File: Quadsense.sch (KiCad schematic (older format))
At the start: 45 parts, among them IC1 BME280, IC2 AP7330, IC3 ADC_LTC2497, P1 CONN_6, P2 CONN_6, P3 CONN_6, P4 CONN_6, P5 CONN_8, Q1 AO3418

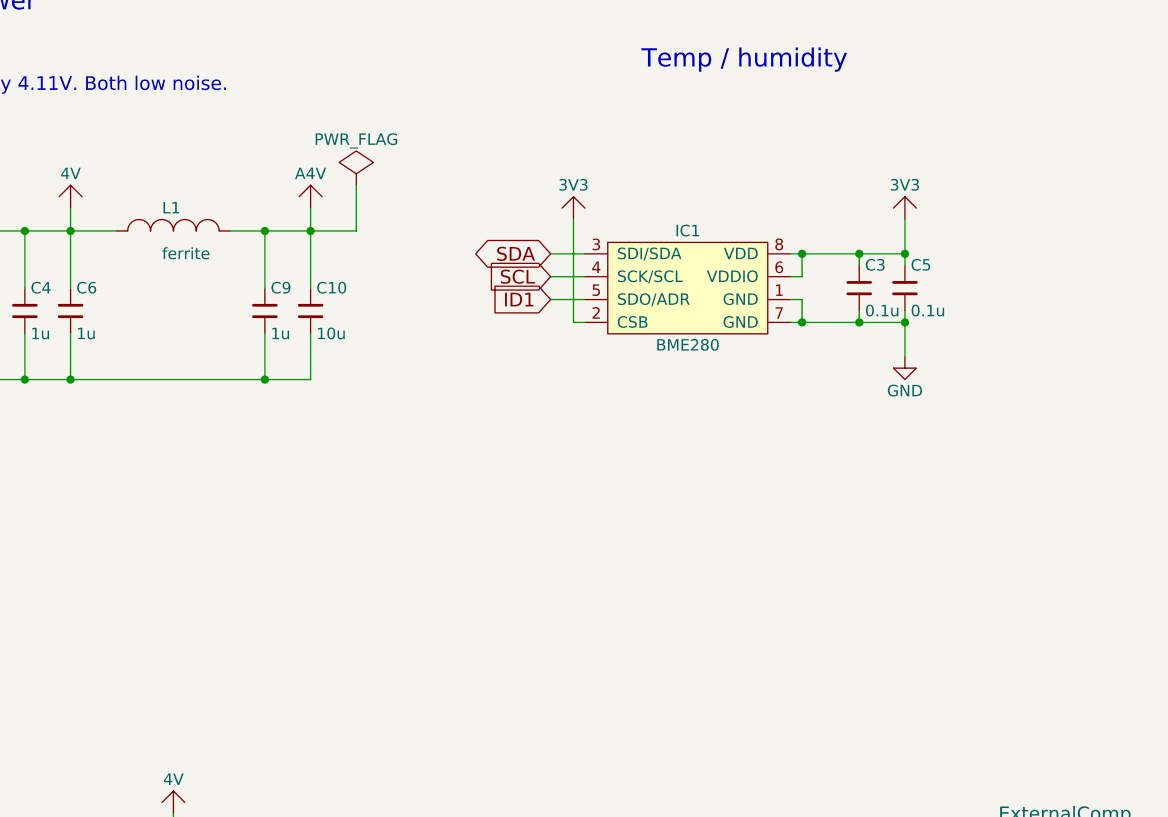
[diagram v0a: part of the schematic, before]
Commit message: Added second BME280, fixed footprints, better analog decoupling, resized module board
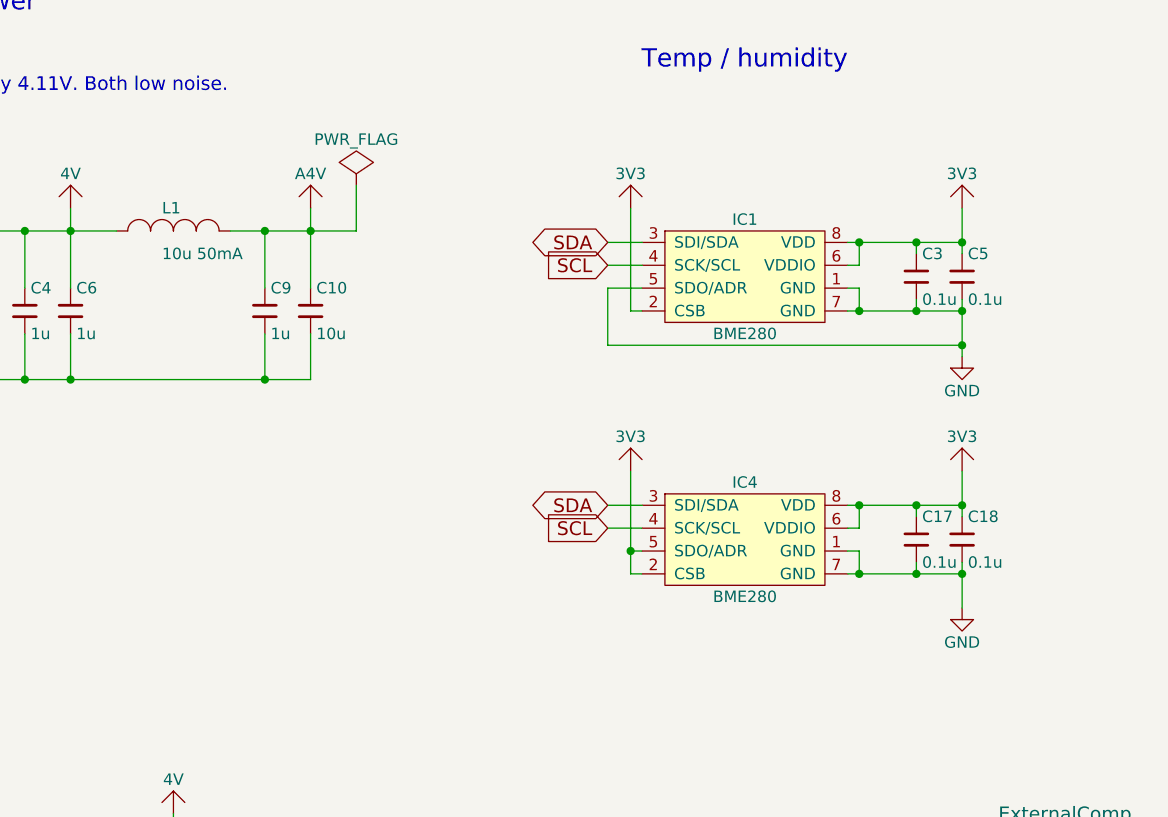
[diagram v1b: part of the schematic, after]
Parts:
- added C17, C18: 0.1u, everykey:0603, symbol C
- added IC4: BME280, everykey:BME280, symbol BME280
- L1: value ferrite -> 10u 50mA
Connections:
- net 3V3: now also C17.1, C18.1, IC4.2 (CSB), IC4.5 (SDO/ADR), IC4.6 (VDDIO), IC4.8 (VDD)
- net GND: now also IC1.5 (SDO/ADR), C17.2, C18.2, IC4.1 (GND), IC4.7 (GND)
- net ID1: no longer IC1.5 (SDO/ADR)
- net SCL: now also IC4.4 (SCK/SCL)
- net SDA: now also IC4.3 (SDI/SDA)
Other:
- moved on the sheet: C3, C5, IC1

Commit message: Saved files
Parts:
- L1: value 10u 50mA -> 22u 50mA; footprint everykey:0603 -> everykey:0805
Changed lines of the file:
@@
 $EndComp
 $Comp
-L GND #PWR7
+L GND #PWR01
 U 1 1 5C6461C4
 P 4900 2550
-F 0 "#PWR7" H 4925 2600 50  0001 C CNN
+F 0 "#PWR01" H 4925 2600 50  0001 C CNN
 F 1 "GND" H 4900 2400 50  0000 C CNN
 F 2 "" H 4900 2550 60  0000 C CNN
@@
 $EndComp
 $Comp
-L 5V #PWR6
+L 5V #PWR02
 U 1 1 5C6461DA
 P 3800 1750
-F 0 "#PWR6" H 3825 1700 60  0001 C CNN
+F 0 "#PWR02" H 3825 1700 60  0001 C CNN
 F 1 "5V" H 3800 1900 50  0000 C CNN
 F 2 "" H 3800 1750 60  0000 C CNN
@@
 $EndComp
 $Comp
-L GND #PWR10
+L GND #PWR03
 U 1 1 5C6480D4
 P 5800 6850
-F 0 "#PWR10" H 5825 6900 50  0001 C CNN
+F 0 "#PWR03" H 5825 6900 50  0001 C CNN
 F 1 "GND" H 5800 6700 50  0000 C CNN
 F 2 "" H 5800 6850 60  0000 C CNN
@@
 $EndComp
 $Comp
-L 3V3 #PWR15
+L 3V3 #PWR04
 U 1 1 5C6545DA
 P 9700 1750
-F 0 "#PWR15" H 9725 1700 60  0001 C CNN
+F 0 "#PWR04" H 9725 1700 60  0001 C CNN
 F 1 "3V3" H 9700 1900 50  0000 C CNN
 F 2 "" H 9700 1750 60  0000 C CNN
@@
 $EndComp
 $Comp
-L GND #PWR16
+L GND #PWR05
 U 1 1 5C65462E
 P 9700 2400
-F 0 "#PWR16" H 9725 2450 50  0001 C CNN
+F 0 "#PWR05" H 9725 2450 50  0001 C CNN
 F 1 "GND" H 9700 2250 50  0000 C CNN
 F 2 "" H 9700 2400 60  0000 C CNN
@@
 $EndComp
 $Comp
-L 3V3 #PWR13
+L 3V3 #PWR06
 U 1 1 5C654F38
 P 8250 1750
-F 0 "#PWR13" H 8275 1700 60  0001 C CNN
+F 0 "#PWR06" H 8275 1700 60  0001 C CNN
 F 1 "3V3" H 8250 1900 50  0000 C CNN
 F 2 "" H 8250 1750 60  0000 C CNN
@@
 P 6250 1850
 F 0 "L1" H 6200 1950 50  0000 L CNN
-F 1 "10u 50mA" H 6200 1750 50  0000 L CNN
-F 2 "everykey:0603" H 6288 1700 50  0001 C CNN
+F 1 "22u 50mA" H 6200 1750 50  0000 L CNN
+F 2 "everykey:0805" H 6288 1700 50  0001 C CNN
 F 3 "" H 6250 1850 50  0000 C CNN
 	1    6250 1850
@@
 3V3\n5V\nGND\nID1\nSCL\nID2\nSDA\nEN
 $Comp
-L GND #PWR3
+L GND #PWR07
 U 1 1 5C6F1ACC
 P 1650 2600
-F 0 "#PWR3" H 1675 2650 50  0001 C CNN
+F 0 "#PWR07" H 1675 2650 50  0001 C CNN
 F 1 "GND" H 1650 2450 50  0000 C CNN
 F 2 "" H 1650 2600 60  0000 C CNN
@@
 $EndComp
 $Comp
-L 3V3 #PWR4
+L 3V3 #PWR08
 U 1 1 5C6F1B4C
 P 1700 1550
-F 0 "#PWR4" H 1725 1500 60  0001 C CNN
+F 0 "#PWR08" H 1725 1500 60  0001 C CNN
 F 1 "3V3" H 1700 1700 50  0000 C CNN
 F 2 "" H 1700 1550 60  0000 C CNN
@@
 $EndComp
 $Comp
-L 5V #PWR1
+L 5V #PWR09
 U 1 1 5C6F1BCC
 P 1550 1550
-F 0 "#PWR1" H 1575 1500 60  0001 C CNN
+F 0 "#PWR09" H 1575 1500 60  0001 C CNN
 F 1 "5V" H 1550 1700 50  0000 C CNN
 F 2 "" H 1550 1550 60  0000 C CNN
@@
 $EndComp
 $Comp
-L GND #PWR5
+L GND #PWR010
 U 1 1 5C6F649C
 P 1950 7250
-F 0 "#PWR5" H 1975 7300 50  0001 C CNN
+F 0 "#PWR010" H 1975 7300 50  0001 C CNN
 F 1 "GND" H 1950 7100 50  0000 C CNN
 F 2 "" H 1950 7250 60  0000 C CNN
@@
 	8300 2100 8150 2100
 $Comp
-L PWR_FLAG #FLAG4
+L PWR_FLAG #FLAG011
 U 1 1 5C6FD365
 P 7050 1650
-F 0 "#FLAG4" H 7050 1750 50  0001 C CNN
+F 0 "#FLAG011" H 7050 1750 50  0001 C CNN
 F 1 "PWR_FLAG" H 7050 1850 50  0000 C CNN
 F 2 "" H 7050 1650 60  0000 C CNN
@@
 	7050 1850 7050 1650
 $Comp
-L PWR_FLAG #FLAG1
+L PWR_FLAG #FLAG012
 U 1 1 5C6FD994
 P 1400 1500
-F 0 "#FLAG1" H 1400 1600 50  0001 C CNN
+F 0 "#FLAG012" H 1400 1600 50  0001 C CNN
 F 1 "PWR_FLAG" H 1400 1700 50  0000 C CNN
 F 2 "" H 1400 1500 60  0000 C CNN
@@
 $EndComp
 $Comp
-L PWR_FLAG #FLAG2
+L PWR_FLAG #FLAG013
 U 1 1 5C6FDA3C
 P 1850 2650
-F 0 "#FLAG2" H 1850 2750 50  0001 C CNN
+F 0 "#FLAG013" H 1850 2750 50  0001 C CNN
 F 1 "PWR_FLAG" H 1850 2850 50  0000 C CNN
 F 2 "" H 1850 2650 60  0000 C CNN
@@
 Connection ~ 5300 5950
 $Comp
-L 4V #PWR9
+L 4V #PWR014
 U 1 1 5C706294
 P 5800 1750
-F 0 "#PWR9" H 5825 1700 60  0001 C CNN
+F 0 "#PWR014" H 5825 1700 60  0001 C CNN
 F 1 "4V" H 5800 1900 50  0000 C CNN
 F 2 "" H 5800 1750 60  0000 C CNN
@@
 $EndComp
 $Comp
-L A4V #PWR12
+L A4V #PWR015
 U 1 1 5C70635C
 P 6850 1750
-F 0 "#PWR12" H 6875 1700 60  0001 C CNN
+F 0 "#PWR015" H 6875 1700 60  0001 C CNN
 F 1 "A4V" H 6850 1900 50  0000 C CNN
 F 2 "" H 6850 1750 60  0000 C CNN
@@
 $EndComp
 $Comp
-L A4V #PWR8
+L A4V #PWR016
 U 1 1 5C706C1D
 P 5300 4400
-F 0 "#PWR8" H 5325 4350 60  0001 C CNN
+F 0 "#PWR016" H 5325 4350 60  0001 C CNN
 F 1 "A4V" H 5300 4550 50  0000 C CNN
 F 2 "" H 5300 4400 60  0000 C CNN
@@
 $EndComp
 $Comp
-L 4V #PWR11
+L 4V #PWR017
 U 1 1 5C706CE5
 P 6250 4400
-F 0 "#PWR11" H 6275 4350 60  0001 C CNN
+F 0 "#PWR017" H 6275 4350 60  0001 C CNN
 F 1 "4V" H 6250 4550 50  0000 C CNN
 F 2 "" H 6250 4400 60  0000 C CNN
@@
 $EndComp
 $Comp
-L A4V #PWR2
+L A4V #PWR018
 U 1 1 5C706F15
 P 1550 3850
-F 0 "#PWR2" H 1575 3800 60  0001 C CNN
+F 0 "#PWR018" H 1575 3800 60  0001 C CNN
 F 1 "A4V" H 1550 4000 50  0000 C CNN
 F 2 "" H 1550 3850 60  0000 C CNN
@@
 $EndComp
 $Comp
-L PWR_FLAG #FLAG3
+L PWR_FLAG #FLAG019
 U 1 1 5C76DA5F
 P 1900 1500
-F 0 "#FLAG3" H 1900 1600 50  0001 C CNN
+F 0 "#FLAG019" H 1900 1600 50  0001 C CNN
 F 1 "PWR_FLAG" H 1900 1700 50  0000 C CNN
 F 2 "" H 1900 1500 60  0000 C CNN
@@
 $EndComp
 $Comp
-L 3V3 #PWR17
+L 3V3 #PWR020
 U 1 1 5CEE62EE
 P 9700 2900
-F 0 "#PWR17" H 9725 2850 60  0001 C CNN
+F 0 "#PWR020" H 9725 2850 60  0001 C CNN
 F 1 "3V3" H 9700 3050 50  0000 C CNN
 F 2 "" H 9700 2900 60  0000 C CNN
@@
 $EndComp
 $Comp
-L GND #PWR18
+L GND #PWR021
 U 1 1 5CEE62F4
 P 9700 3500
-F 0 "#PWR18" H 9725 3550 50  0001 C CNN
+F 0 "#PWR021" H 9725 3550 50  0001 C CNN
 F 1 "GND" H 9700 3350 50  0000 C CNN
 F 2 "" H 9700 3500 60  0000 C CNN
@@
 $EndComp
 $Comp
-L 3V3 #PWR14
+L 3V3 #PWR022
 U 1 1 5CEE62FA
 P 8250 2900
-F 0 "#PWR14" H 8275 2850 60  0001 C CNN
+F 0 "#PWR022" H 8275 2850 60  0001 C CNN
 F 1 "3V3" H 8250 3050 50  0000 C CNN
 F 2 "" H 8250 2900 60  0000 C CNN

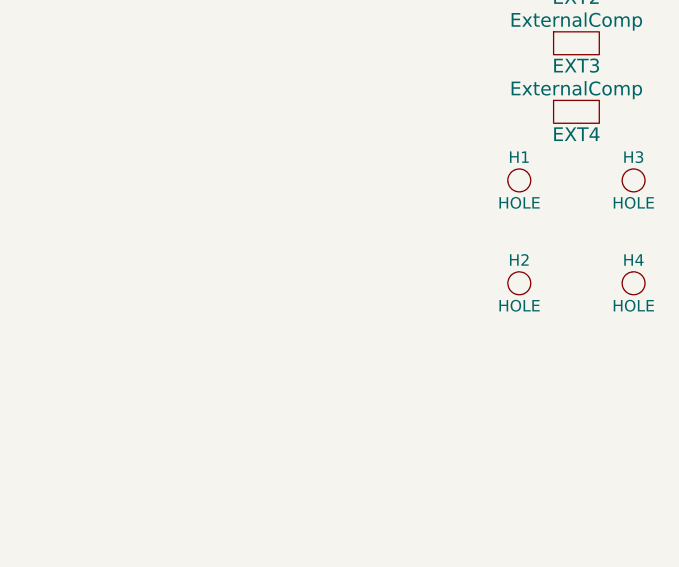
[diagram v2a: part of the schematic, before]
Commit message: Silkscreen fixes
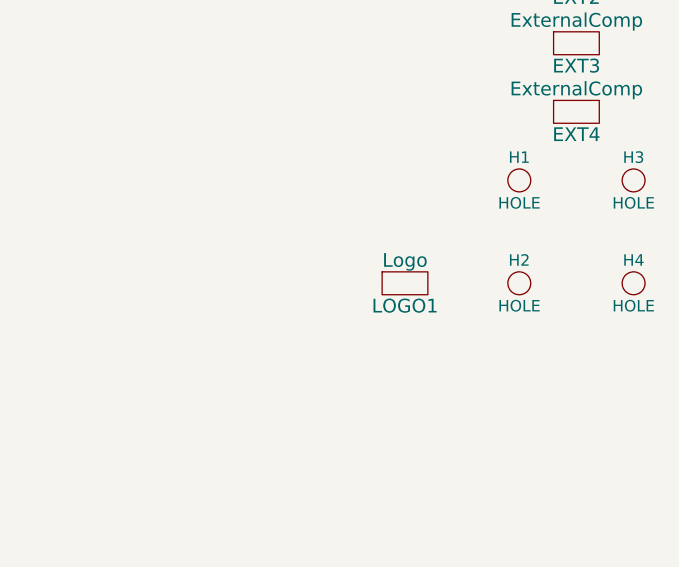
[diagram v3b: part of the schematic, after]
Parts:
- added LOGO1: Logo, symbol Logo
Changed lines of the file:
@@
 EESchema Schematic File Version 2
-LIBS:Quadsense-rescue
 LIBS:everykey
 LIBS:Quadsense-cache
@@
 $EndComp
 $Comp
-L GND #PWR01
+L GND #PWR7
 U 1 1 5C6461C4
 P 4900 2550
-F 0 "#PWR01" H 4925 2600 50  0001 C CNN
+F 0 "#PWR7" H 4925 2600 50  0001 C CNN
 F 1 "GND" H 4900 2400 50  0000 C CNN
 F 2 "" H 4900 2550 60  0000 C CNN
@@
 $EndComp
 $Comp
-L 5V #PWR02
+L 5V #PWR6
 U 1 1 5C6461DA
 P 3800 1750
-F 0 "#PWR02" H 3825 1700 60  0001 C CNN
+F 0 "#PWR6" H 3825 1700 60  0001 C CNN
 F 1 "5V" H 3800 1900 50  0000 C CNN
 F 2 "" H 3800 1750 60  0000 C CNN
@@
 $EndComp
 $Comp
-L GND #PWR03
+L GND #PWR10
 U 1 1 5C6480D4
 P 5800 6850
-F 0 "#PWR03" H 5825 6900 50  0001 C CNN
+F 0 "#PWR10" H 5825 6900 50  0001 C CNN
 F 1 "GND" H 5800 6700 50  0000 C CNN
 F 2 "" H 5800 6850 60  0000 C CNN
@@
 $EndComp
 $Comp
-L 3V3 #PWR04
+L 3V3 #PWR15
 U 1 1 5C6545DA
 P 9700 1750
-F 0 "#PWR04" H 9725 1700 60  0001 C CNN
+F 0 "#PWR15" H 9725 1700 60  0001 C CNN
 F 1 "3V3" H 9700 1900 50  0000 C CNN
 F 2 "" H 9700 1750 60  0000 C CNN
@@
 $EndComp
 $Comp
-L GND #PWR05
+L GND #PWR16
 U 1 1 5C65462E
 P 9700 2400
-F 0 "#PWR05" H 9725 2450 50  0001 C CNN
+F 0 "#PWR16" H 9725 2450 50  0001 C CNN
 F 1 "GND" H 9700 2250 50  0000 C CNN
 F 2 "" H 9700 2400 60  0000 C CNN
@@
 $EndComp
 $Comp
-L 3V3 #PWR06
+L 3V3 #PWR13
 U 1 1 5C654F38
 P 8250 1750
-F 0 "#PWR06" H 8275 1700 60  0001 C CNN
+F 0 "#PWR13" H 8275 1700 60  0001 C CNN
 F 1 "3V3" H 8250 1900 50  0000 C CNN
 F 2 "" H 8250 1750 60  0000 C CNN
@@
 3V3\n5V\nGND\nID1\nSCL\nID2\nSDA\nEN
 $Comp
-L GND #PWR07
+L GND #PWR3
 U 1 1 5C6F1ACC
 P 1650 2600
-F 0 "#PWR07" H 1675 2650 50  0001 C CNN
+F 0 "#PWR3" H 1675 2650 50  0001 C CNN
 F 1 "GND" H 1650 2450 50  0000 C CNN
 F 2 "" H 1650 2600 60  0000 C CNN
@@
 $EndComp
 $Comp
-L 3V3 #PWR08
+L 3V3 #PWR4
 U 1 1 5C6F1B4C
 P 1700 1550
-F 0 "#PWR08" H 1725 1500 60  0001 C CNN
+F 0 "#PWR4" H 1725 1500 60  0001 C CNN
 F 1 "3V3" H 1700 1700 50  0000 C CNN
 F 2 "" H 1700 1550 60  0000 C CNN
@@
 $EndComp
 $Comp
-L 5V #PWR09
+L 5V #PWR1
 U 1 1 5C6F1BCC
 P 1550 1550
-F 0 "#PWR09" H 1575 1500 60  0001 C CNN
+F 0 "#PWR1" H 1575 1500 60  0001 C CNN
 F 1 "5V" H 1550 1700 50  0000 C CNN
 F 2 "" H 1550 1550 60  0000 C CNN
@@
 $EndComp
 $Comp
-L GND #PWR010
+L GND #PWR5
 U 1 1 5C6F649C
 P 1950 7250
-F 0 "#PWR010" H 1975 7300 50  0001 C CNN
+F 0 "#PWR5" H 1975 7300 50  0001 C CNN
 F 1 "GND" H 1950 7100 50  0000 C CNN
 F 2 "" H 1950 7250 60  0000 C CNN
@@
 	8300 2100 8150 2100
 $Comp
-L PWR_FLAG #FLAG011
+L PWR_FLAG #FLAG4
 U 1 1 5C6FD365
 P 7050 1650
-F 0 "#FLAG011" H 7050 1750 50  0001 C CNN
+F 0 "#FLAG4" H 7050 1750 50  0001 C CNN
 F 1 "PWR_FLAG" H 7050 1850 50  0000 C CNN
 F 2 "" H 7050 1650 60  0000 C CNN
@@
 	7050 1850 7050 1650
 $Comp
-L PWR_FLAG #FLAG012
+L PWR_FLAG #FLAG1
 U 1 1 5C6FD994
 P 1400 1500
-F 0 "#FLAG012" H 1400 1600 50  0001 C CNN
+F 0 "#FLAG1" H 1400 1600 50  0001 C CNN
 F 1 "PWR_FLAG" H 1400 1700 50  0000 C CNN
 F 2 "" H 1400 1500 60  0000 C CNN
@@
 $EndComp
 $Comp
-L PWR_FLAG #FLAG013
+L PWR_FLAG #FLAG2
 U 1 1 5C6FDA3C
 P 1850 2650
-F 0 "#FLAG013" H 1850 2750 50  0001 C CNN
+F 0 "#FLAG2" H 1850 2750 50  0001 C CNN
 F 1 "PWR_FLAG" H 1850 2850 50  0000 C CNN
 F 2 "" H 1850 2650 60  0000 C CNN
@@
 Connection ~ 5300 5950
 $Comp
-L 4V #PWR014
+L 4V #PWR9
 U 1 1 5C706294
 P 5800 1750
-F 0 "#PWR014" H 5825 1700 60  0001 C CNN
+F 0 "#PWR9" H 5825 1700 60  0001 C CNN
 F 1 "4V" H 5800 1900 50  0000 C CNN
 F 2 "" H 5800 1750 60  0000 C CNN
@@
 $EndComp
 $Comp
-L A4V #PWR015
+L A4V #PWR12
 U 1 1 5C70635C
 P 6850 1750
-F 0 "#PWR015" H 6875 1700 60  0001 C CNN
+F 0 "#PWR12" H 6875 1700 60  0001 C CNN
 F 1 "A4V" H 6850 1900 50  0000 C CNN
 F 2 "" H 6850 1750 60  0000 C CNN
@@
 $EndComp
 $Comp
-L A4V #PWR016
+L A4V #PWR8
 U 1 1 5C706C1D
 P 5300 4400
-F 0 "#PWR016" H 5325 4350 60  0001 C CNN
+F 0 "#PWR8" H 5325 4350 60  0001 C CNN
 F 1 "A4V" H 5300 4550 50  0000 C CNN
 F 2 "" H 5300 4400 60  0000 C CNN
@@
 $EndComp
 $Comp
-L 4V #PWR017
+L 4V #PWR11
 U 1 1 5C706CE5
 P 6250 4400
-F 0 "#PWR017" H 6275 4350 60  0001 C CNN
+F 0 "#PWR11" H 6275 4350 60  0001 C CNN
 F 1 "4V" H 6250 4550 50  0000 C CNN
 F 2 "" H 6250 4400 60  0000 C CNN
@@
 $EndComp
 $Comp
-L A4V #PWR018
+L A4V #PWR2
 U 1 1 5C706F15
 P 1550 3850
-F 0 "#PWR018" H 1575 3800 60  0001 C CNN
+F 0 "#PWR2" H 1575 3800 60  0001 C CNN
 F 1 "A4V" H 1550 4000 50  0000 C CNN
 F 2 "" H 1550 3850 60  0000 C CNN
@@
 $EndComp
 $Comp
-L PWR_FLAG #FLAG019
+L PWR_FLAG #FLAG3
 U 1 1 5C76DA5F
 P 1900 1500
-F 0 "#FLAG019" H 1900 1600 50  0001 C CNN
+F 0 "#FLAG3" H 1900 1600 50  0001 C CNN
 F 1 "PWR_FLAG" H 1900 1700 50  0000 C CNN
 F 2 "" H 1900 1500 60  0000 C CNN
@@
 $EndComp
 $Comp
-L 3V3 #PWR020
+L 3V3 #PWR17
 U 1 1 5CEE62EE
 P 9700 2900
-F 0 "#PWR020" H 9725 2850 60  0001 C CNN
+F 0 "#PWR17" H 9725 2850 60  0001 C CNN
 F 1 "3V3" H 9700 3050 50  0000 C CNN
 F 2 "" H 9700 2900 60  0000 C CNN
@@
 $EndComp
 $Comp
-L GND #PWR021
+L GND #PWR18
 U 1 1 5CEE62F4
 P 9700 3500
-F 0 "#PWR021" H 9725 3550 50  0001 C CNN
+F 0 "#PWR18" H 9725 3550 50  0001 C CNN
 F 1 "GND" H 9700 3350 50  0000 C CNN
 F 2 "" H 9700 3500 60  0000 C CNN
@@
 $EndComp
 $Comp
-L 3V3 #PWR022
+L 3V3 #PWR14
 U 1 1 5CEE62FA
 P 8250 2900
-F 0 "#PWR022" H 8275 2850 60  0001 C CNN
+F 0 "#PWR14" H 8275 2850 60  0001 C CNN
 F 1 "3V3" H 8250 3050 50  0000 C CNN
 F 2 "" H 8250 2900 60  0000 C CNN
@@
 	8300 3250 8250 3250
 Connection ~ 8250 3250
+$Comp
+L Logo LOGO1
+U 1 1 5CF7FDEB
+P 9400 6150
+F 0 "LOGO1" H 9400 6050 60  0000 C CNN
+F 1 "Logo" H 9400 6250 60  0000 C CNN
+F 2 "" H 9400 6300 60  0001 C CNN
+F 3 "" H 9400 6300 60  0001 C CNN
+	1    9400 6150
+	1    0    0    -1
+$EndComp
 $EndSCHEMATC
